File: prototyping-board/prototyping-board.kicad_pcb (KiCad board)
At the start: 2 copper layers, 80 x 80 mm, 45 parts, among them J1 Conn_01x02, J10 Conn_01x02, J11 Conn_01x03, J12 Conn_01x03, J13 Conn_01x03, J14 Conn_01x03, J15 Conn_01x03, J16 Conn_01x03, J17 Conn_01x03, J18 Conn_01x03, J19 Conn_01x03, J2 Conn_01x02, J20 Conn_01x03, J21 Conn_01x03, J22 Conn_01x03, J23 Conn_01x06, J24 Conn_01x06, J25 Conn_01x04, J26 Conn_01x04, J27 Conn_01x05, J28 Conn_01x05, J29 Conn_01x05, J3 Conn_01x02, J30 Conn_01x04, J31 Conn_01x04, J32 Conn_01x04, J33 Conn_01x03, J34 Conn_01x03, J35 Conn_01x03, J36 Conn_01x02, J37 Conn_01x02, J38 Conn_01x02, J4 Conn_01x02, J5 Conn_01x02, J6 Conn_01x02, J7 Conn_01x02, J8 Conn_01x02, J9 Conn_01x02, U1 MEGA_PRO_EMBED_CH340G___ATMEG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

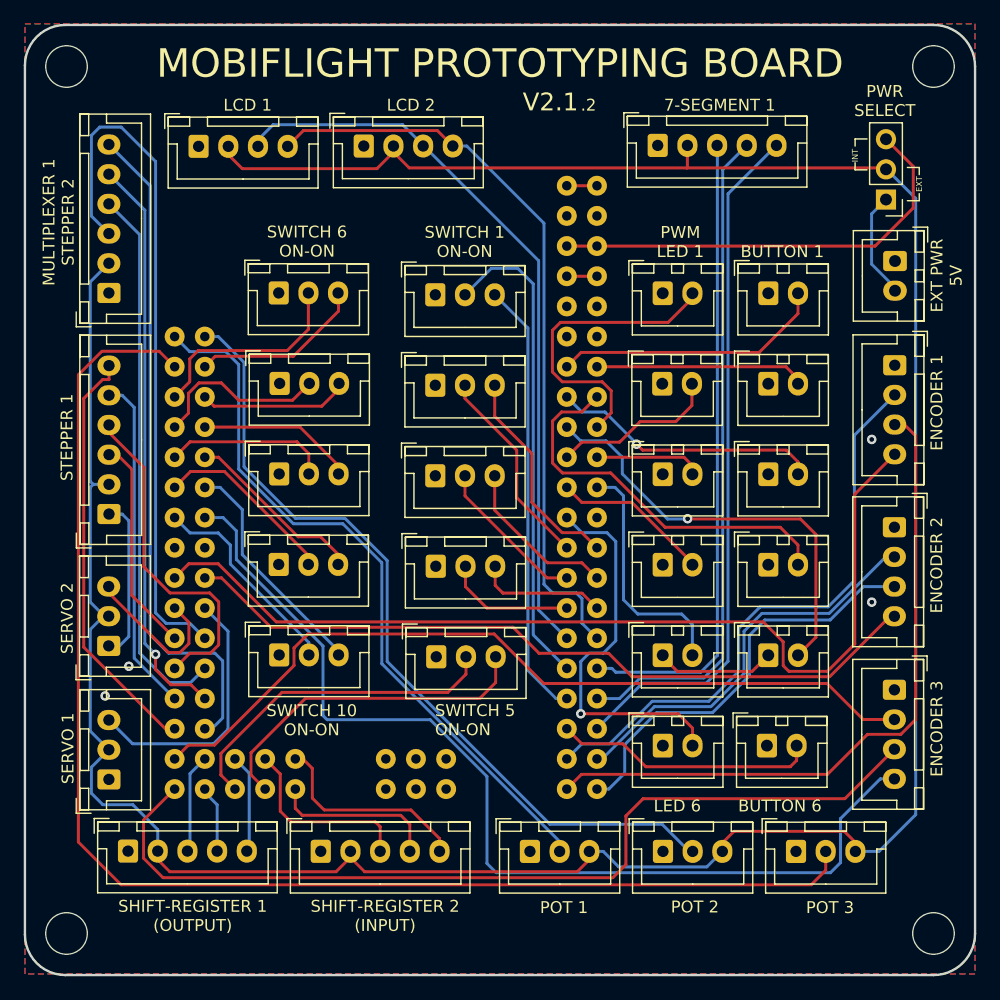
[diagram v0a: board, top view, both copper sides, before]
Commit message: Prototype without power jumper
* add diode, add 4th Encoder, new position of PWR

* PWR connector in red, some optimazations

* ENC4 switch to Button 6

* update readme with shared pins

* LED6 to D13, ENC4 switch to D12

* update MegaMini symbol

* add a reset button, update readme accordingly

* add board config for board version 2.2

* fix wrong spelling
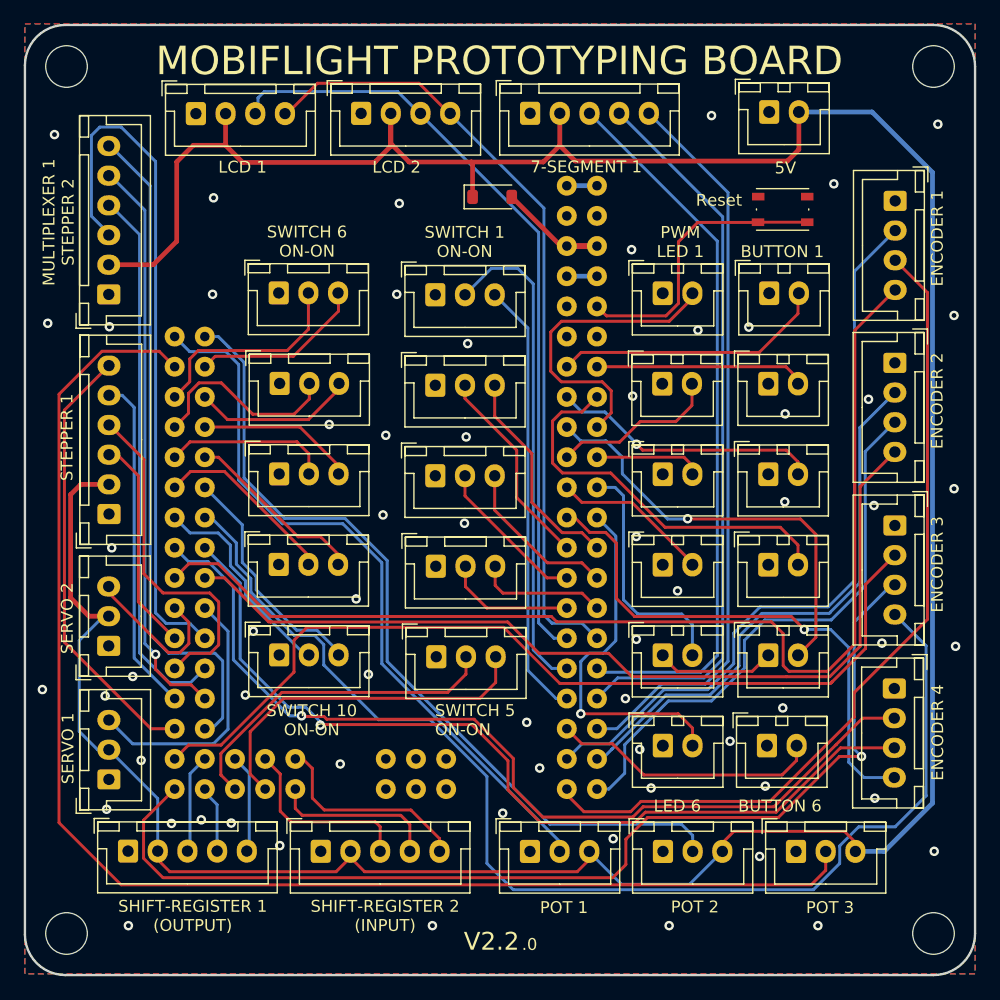
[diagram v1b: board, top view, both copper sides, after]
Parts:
- removed JP1: Jumper_3_Open, Connector_PinHeader_2.54mm:PinHeader_1x03_P2.54mm_Vertical
- added D1: D_Schottky_B5819W-SL, Diode_SMD:D_SOD-123, F.Cu at (64.3, 38.5)
- added J39: Conn_01x04, Connector_JST:JST_XH_B4B-XH-A_1x04_P2.50mm_Vertical, F.Cu at (98.2, 79.9)
- added SW1: Switch_SMD_5x5_Wuerth, MobiFlight:SW_Push_1P1T_NO_Vertical_Wuerth_434133025816, F.Cu at (88.8, 39.5)
- G***: footprint footprints:mobiflight-logo-12 -> MobiFlight:MobiFlight-Logo-Small
- moved G*** 22.0 mm to (87.6, 41.2), turned to 90 degrees
- moved J36 16.4 mm to (87.7, 31.3), turned to 0 degrees
- moved J30 13.8 mm to (98.3, 38.8)
- moved J32 13.8 mm to (98.2, 66.1)
- moved J31 13.8 mm to (98.2, 52.5)
- moved J29 11.1 mm to (67.5, 31.4)
- moved J25 2.77 mm to (39.4, 31.5)
- moved J26 2.76 mm to (53.3, 31.4)
- moved J24 0.12 mm to (32.1, 46.7)
- moved J1 0.07 mm to (87.7, 46.6)
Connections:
- J36 pad 2: Net-(J36-Pin_2) -> +5VD
- U1 pad 3V3_1: unconnected-(U1-3V3-Pad3V3_1)_1 -> unconnected-(U1-3V3-Pad3V3_1)
- U1 pad A14: unconnected-(U1-PadA14) -> ENC4-A
- U1 pad A15: unconnected-(U1-PadA15) -> ENC4-B
- U1 pad D12: LED06 -> ENC4-SW
- U1 pad D13: unconnected-(U1-PadD13) -> LED06
- U1 pad RST: unconnected-(U1-PadRST) -> Reset
- U1 pad VIN_1: unconnected-(U1-VIN-PadVIN_1)_1 -> unconnected-(U1-VIN-PadVIN_1)
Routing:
- net ENC4-A: track 0.00 -> 78.5 mm, vias 0 -> 1
- net ENC4-B: track 0.00 -> 75.7 mm, vias 0 -> 1
- net ENC4-SW: track 0.00 -> 45.0 mm, vias 0 -> 1
- net +5V: track 37.2 -> 11.4 mm
- net Reset: track 0.00 -> 24.3 mm
- net +5VD: track 246.3 -> 270.4 mm
- net ENC3-SW: track 85.0 -> 101.6 mm
- net ENC1-SW: track 81.0 -> 95.3 mm
- net GND: track 23.8 -> 10.1 mm, vias 4 -> 63
- net ENC2-SW: track 63.6 -> 77.3 mm
- net ENC1-A: track 49.6 -> 62.8 mm
- net ENC1-B: track 57.8 -> 70.7 mm
- net ENC2-A: track 34.2 -> 47.0 mm
- net ENC2-B: track 35.5 -> 48.1 mm
- net ENC3-B: track 77.7 -> 89.8 mm, vias 0 -> 1
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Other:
- board text added: ".0"
- board text added: "???"
- board text added: "A14"
- board text added: "A15"
- board text added: "ENCODER 4"
- board text added: "Reset"
- board text added: "V2.2"
- board text removed: ".2"
- board text removed: "EXT"
- board text removed: "EXT PWR 5V"
- board text removed: "INT"
- board text removed: "PWR SELECT"
- board text removed: "V2.1"
